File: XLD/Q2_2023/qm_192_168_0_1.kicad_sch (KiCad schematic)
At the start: 113 parts, among them T1 Terminator, T10 Terminator, T11 Terminator, T12 Terminator, T13 Terminator, T14 Terminator, T15 Terminator, T16 Terminator, T2 Terminator, T3 Terminator, T4 Terminator, T5 Terminator, T6 Terminator, T7 Terminator, T8 Terminator, T9 Terminator

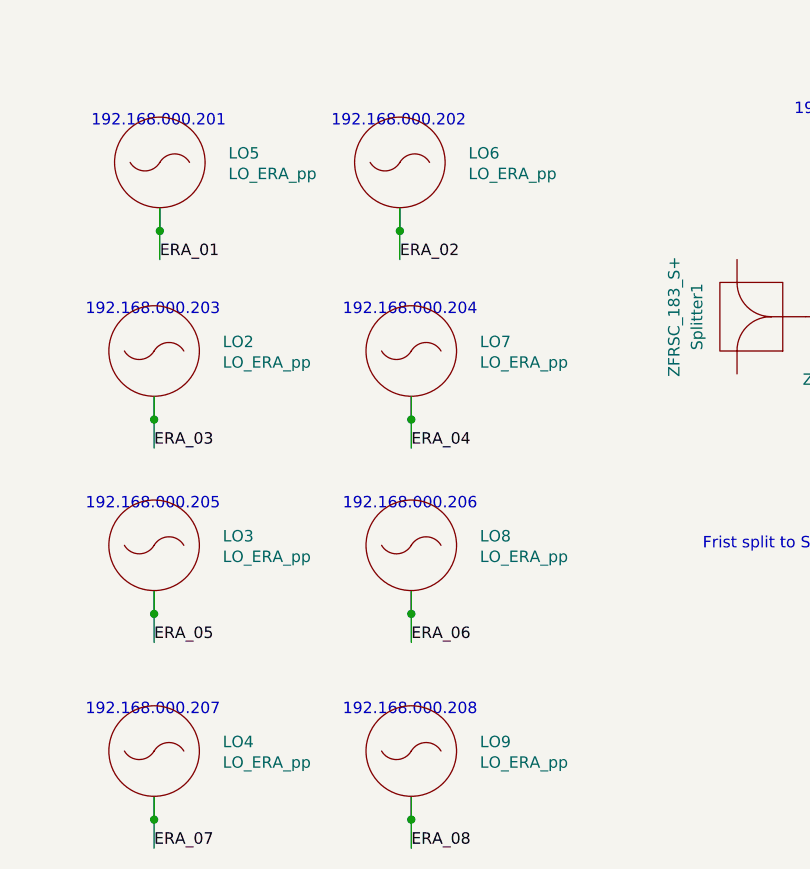
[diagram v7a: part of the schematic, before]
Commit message: various fixes
swap L3-20 with L2-17 in qblox
change ip of Lo18 to 192.168.0.208 (tii1q_b4 twpa pump) and type to ERA
rename LO_ERA_pp to LO_ERA
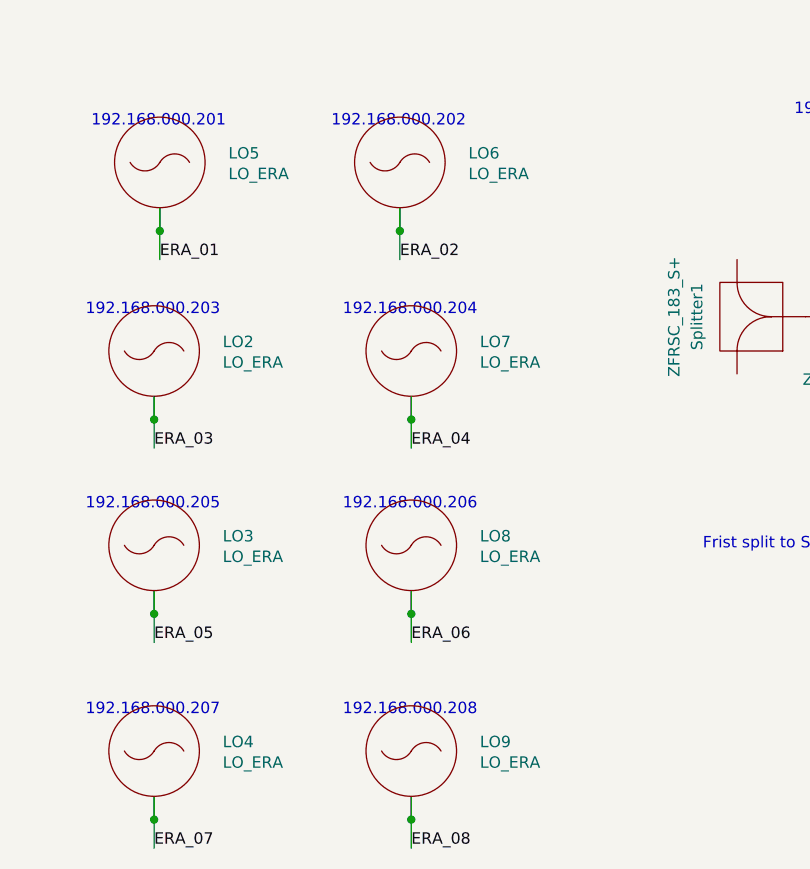
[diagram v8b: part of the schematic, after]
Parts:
- LO2, LO3, LO4, LO5, LO6, LO7, LO8, LO9: value LO_ERA_pp -> LO_ERA; symbol Quantum Computing:LO_ERA_pp -> Quantum Computing:LO_ERA
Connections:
- net at Splitter17.: now also Splitter18.; no longer Splitter16.
- net at Splitter18.: no longer Splitter17.
- net at Splitter6.: now also Splitter5.; no longer Splitter8.
- net at Splitter10.: now also Splitter9.; no longer Splitter8.
- net at Splitter22.: no longer Splitter21.
- net at Splitter20.: no longer Splitter21.
- net at Splitter7.: no longer Splitter6.
- net at Splitter5.: no longer Splitter6.
- net at Splitter14.: now also Splitter13.
- net at Splitter13.: now also Splitter12.; no longer Splitter14.
- net at Splitter11.: now also Splitter10.
- net at Splitter12.: no longer Splitter13.
- net at Splitter1.: no longer Splitter2.
- net at Splitter3.: no longer Splitter2.
- net at Splitter4.: now also Splitter3.
- new net: Splitter16., Splitter17.
- new net: Splitter15., Splitter17.
- new net: Splitter6., Splitter8.
- new net: Splitter10., Splitter8.
- new net: Splitter21., Splitter22.
- new net: Splitter20., Splitter21.
- new net: Splitter6., Splitter7.
- new net: Splitter13., Splitter15.
- new net: Splitter1., Splitter2.
- new net: Splitter2., Splitter3.
- now unconnected: Splitter3.
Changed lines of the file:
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@@
     )
   )
-  (symbol (lib_id "Quantum Computing:LO_ERA_pp") (at 187.96 344.17 0) (unit 1)
+  (symbol (lib_id "Quantum Computing:LO_ERA") (at 187.96 344.17 0) (unit 1)
     (in_bom yes) (on_board no) (dnp no) (fields_autoplaced)
     (property "Reference" "LO7" (at 195.58 343.154 0)
       (effects (font (size 1.27 1.27)) (justify left))
     )
-    (property "Value" "LO_ERA_pp" (at 195.58 345.44 0)
+    (property "Value" "LO_ERA" (at 195.58 345.44 0)
       (effects (font (size 1.27 1.27)) (justify left))
     )
@@
     )
   )
-  (symbol (lib_id "Quantum Computing:LO_ERA_pp") (at 159.385 365.76 0) (unit 1)
+  (symbol (lib_id "Quantum Computing:LO_ERA") (at 159.385 365.76 0) (unit 1)
     (in_bom yes) (on_board no) (dnp no) (fields_autoplaced)
     (property "Reference" "LO3" (at 167.005 364.744 0)
       (effects (font (size 1.27 1.27)) (justify left))
     )
-    (property "Value" "LO_ERA_pp" (at 167.005 367.03 0)
+    (property "Value" "LO_ERA" (at 167.005 367.03 0)
       (effects (font (size 1.27 1.27)) (justify left))
     )
@@
     )
   )
-  (symbol (lib_id "Quantum Computing:LO_ERA_pp") (at 187.96 365.76 0) (unit 1)
+  (symbol (lib_id "Quantum Computing:LO_ERA") (at 187.96 365.76 0) (unit 1)
     (in_bom yes) (on_board no) (dnp no) (fields_autoplaced)
     (property "Reference" "LO8" (at 195.58 364.744 0)
       (effects (font (size 1.27 1.27)) (justify left))
     )
-    (property "Value" "LO_ERA_pp" (at 195.58 367.03 0)
+    (property "Value" "LO_ERA" (at 195.58 367.03 0)
       (effects (font (size 1.27 1.27)) (justify left))
     )
@@
     )
   )
-  (symbol (lib_id "Quantum Computing:LO_ERA_pp") (at 186.69 323.215 0) (unit 1)
+  (symbol (lib_id "Quantum Computing:LO_ERA") (at 186.69 323.215 0) (unit 1)
     (in_bom yes) (on_board no) (dnp no) (fields_autoplaced)
     (property "Reference" "LO6" (at 194.31 322.199 0)
       (effects (font (size 1.27 1.27)) (justify left))
     )
-    (property "Value" "LO_ERA_pp" (at 194.31 324.485 0)
+    (property "Value" "LO_ERA" (at 194.31 324.485 0)
       (effects (font (size 1.27 1.27)) (justify left))
     )
@@
     )
   )
-  (symbol (lib_id "Quantum Computing:LO_ERA_pp") (at 187.96 388.62 0) (unit 1)
+  (symbol (lib_id "Quantum Computing:LO_ERA") (at 187.96 388.62 0) (unit 1)
     (in_bom yes) (on_board no) (dnp no) (fields_autoplaced)
     (property "Reference" "LO9" (at 195.58 387.604 0)
       (effects (font (size 1.27 1.27)) (justify left))
     )
-    (property "Value" "LO_ERA_pp" (at 195.58 389.89 0)
+    (property "Value" "LO_ERA" (at 195.58 389.89 0)
       (effects (font (size 1.27 1.27)) (justify left))
     )
@@
     )
   )
-  (symbol (lib_id "Quantum Computing:LO_ERA_pp") (at 159.385 344.17 0) (unit 1)
+  (symbol (lib_id "Quantum Computing:LO_ERA") (at 159.385 344.17 0) (unit 1)
     (in_bom yes) (on_board no) (dnp no) (fields_autoplaced)
     (property "Reference" "LO2" (at 167.005 343.154 0)
       (effects (font (size 1.27 1.27)) (justify left))
     )
-    (property "Value" "LO_ERA_pp" (at 167.005 345.44 0)
+    (property "Value" "LO_ERA" (at 167.005 345.44 0)
       (effects (font (size 1.27 1.27)) (justify left))
     )
@@
     )
   )
-  (symbol (lib_id "Quantum Computing:LO_ERA_pp") (at 160.02 323.215 0) (unit 1)
+  (symbol (lib_id "Quantum Computing:LO_ERA") (at 160.02 323.215 0) (unit 1)
     (in_bom yes) (on_board no) (dnp no) (fields_autoplaced)
     (property "Reference" "LO5" (at 167.64 322.199 0)
       (effects (font (size 1.27 1.27)) (justify left))
     )
-    (property "Value" "LO_ERA_pp" (at 167.64 324.485 0)
+    (property "Value" "LO_ERA" (at 167.64 324.485 0)
       (effects (font (size 1.27 1.27)) (justify left))
     )
@@
     )
   )
-  (symbol (lib_id "Quantum Computing:LO_ERA_pp") (at 159.385 388.62 0) (unit 1)
+  (symbol (lib_id "Quantum Computing:LO_ERA") (at 159.385 388.62 0) (unit 1)
     (in_bom yes) (on_board no) (dnp no) (fields_autoplaced)
     (property "Reference" "LO4" (at 167.005 387.604 0)
       (effects (font (size 1.27 1.27)) (justify left))
     )
-    (property "Value" "LO_ERA_pp" (at 167.005 389.89 0)
-      (effects (font (size 1.27 1.27)) (justify left))
-    )
+    (property "Value" "LO_ERA" (at 167.005 389.89 0)
+      (effects (font (size 1.27 1.27)) (justify left))
+    )
